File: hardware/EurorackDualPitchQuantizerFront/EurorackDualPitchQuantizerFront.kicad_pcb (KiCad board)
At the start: 2 copper layers, 48 x 110 mm, 67 parts, among them J1 Conn_01x12_Male, J10 Conn_01x04_Male, J11 AudioJack2, J12 AudioJack2, J13 Conn_01x02_Male, J2 Conn_01x01_Male, J3 Conn_01x02_Male, J4 Conn_01x02_Male, J5 AudioJack2, J6 AudioJack2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

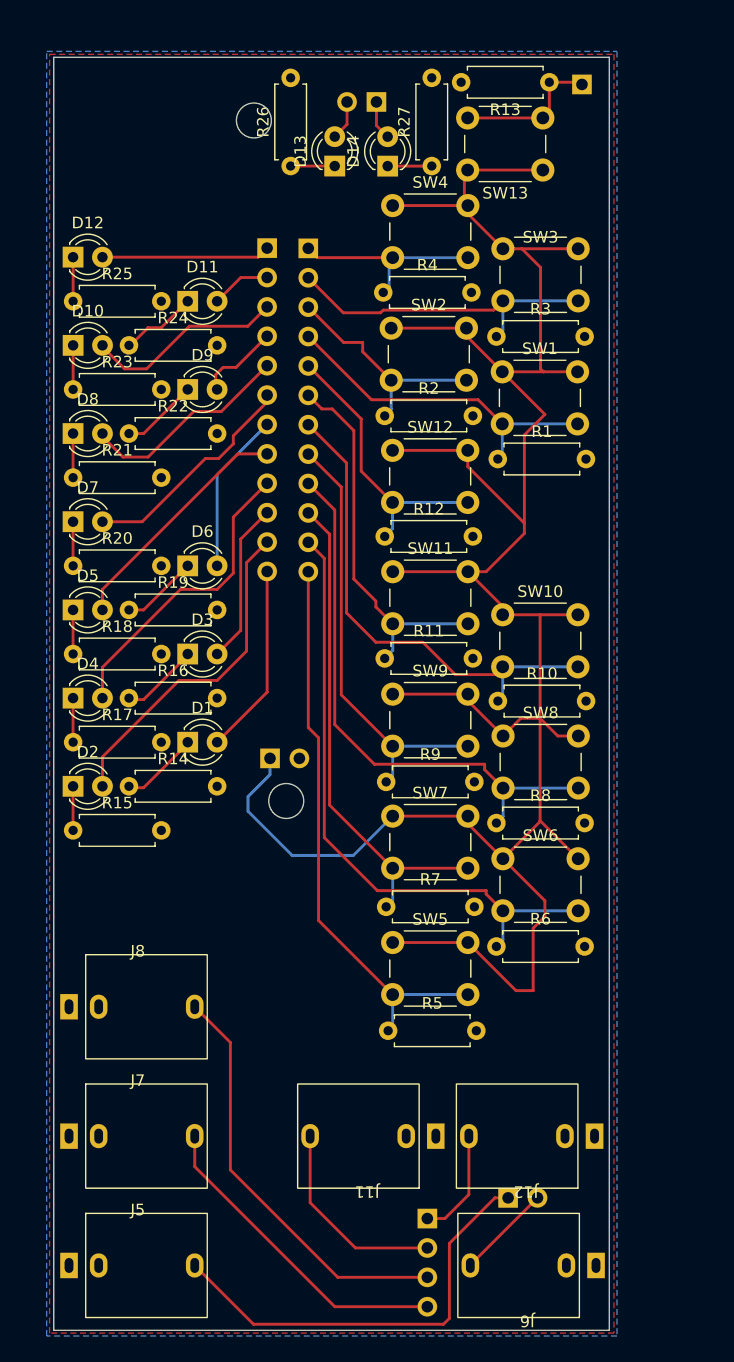
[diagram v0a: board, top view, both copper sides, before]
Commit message: made another version that is not viable since it is too tall
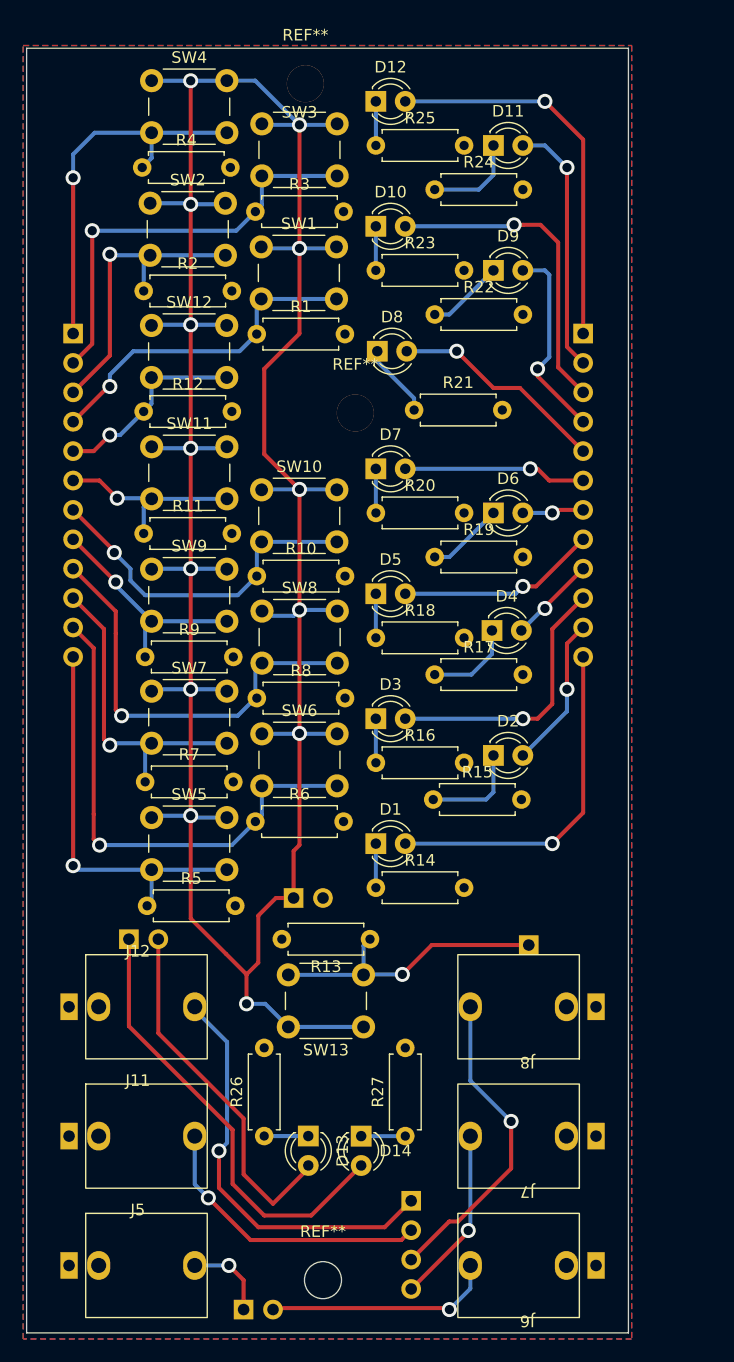
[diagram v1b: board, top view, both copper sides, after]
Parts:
- added REF**: MountingHole_3.2mm_M3, MountingHole:MountingHole_3.2mm_M3, F.Cu at (38.6, 123.4)
- added REF**: MountingHole_3.2mm_M3, MountingHole:MountingHole_3.2mm_M3, F.Cu at (37.1, 20.1)
- added REF**: MountingHole_3.2mm_M3, MountingHole:MountingHole_3.2mm_M3, F.Cu at (41.4, 48.5)
- J11, J12, J5, J6, J7, J8: value AudioJack2 -> AudioJack2_SwitchT
- moved D13 83.8 mm to (37.3, 111.0), turned to -90 degrees
- moved D14 83.8 mm to (41.9, 111.0), turned to -90 degrees
- moved R26 83.8 mm to (33.5, 111.0)
- moved R27 83.8 mm to (45.7, 111.0)
- moved R13 75.6 mm to (42.7, 94.0)
- moved SW13 75.6 mm to (42.1, 101.6)
- moved J13 75.4 mm to (21.8, 94.0), turned to -90 degrees
- moved J2 74.5 mm to (56.4, 94.5)
- moved D4 36.7 mm to (53.2, 67.3)
- moved D2 36.4 mm to (53.3, 78.1)
- moved J12 35.3 mm to (22.6, 99.8), turned to 0 degrees
- moved J7 33.7 mm to (56.3, 111.0), turned to 180 degrees
- moved J8 33.7 mm to (56.3, 99.8), turned to 180 degrees
- moved R17 31.8 mm to (48.3, 71.1)
- moved R15 31.2 mm to (48.1, 81.9)
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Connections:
- J11 pad S: Net-(J10-Pad2) -> GND
- J11 pad T: GND -> Net-(J10-Pad2)
- J12 pad S: Net-(J10-Pad1) -> GND
- J12 pad T: GND -> Net-(J10-Pad1)
- J5 pad S: Net-(J4-Pad1) -> GND
- J5 pad T: GND -> Net-(J4-Pad1)
- J6 pad S: Net-(J4-Pad2) -> GND
- J6 pad T: GND -> Net-(J4-Pad2)
- J7 pad S: Net-(J10-Pad4) -> GND
- J7 pad T: GND -> Net-(J10-Pad4)
- J8 pad S: Net-(J10-Pad3) -> GND
- J8 pad T: GND -> Net-(J10-Pad3)
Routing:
- net +5V: track 218.2 -> 258.5 mm, vias 0 -> 13
- net Net-(D14-Pad2): track 3.40 -> 38.9 mm
- net Net-(J4-Pad1): track 37.5 -> 7.29 mm, vias 0 -> 1
- net Net-(D13-Pad2): track 3.44 -> 31.5 mm
- net Net-(J10-Pad1): track 9.88 -> 36.1 mm, vias 0 -> 1
- net Net-(D12-Pad2): track 14.3 -> 33.5 mm, vias 0 -> 1
- net Net-(D4-Pad2): track 26.3 -> 7.63 mm, vias 0 -> 1
- net Net-(J1-Pad8): track 38.1 -> 19.7 mm, vias 0 -> 1
- net Net-(D11-Pad2): track 5.17 -> 22.1 mm, vias 0 -> 1
- net Net-(J1-Pad10): track 43.8 -> 27.8 mm, vias 0 -> 1
- net Net-(J1-Pad1): track 17.0 -> 32.9 mm, vias 0 -> 1
- net Net-(J1-Pad6): track 33.1 -> 17.2 mm, vias 0 -> 1
- net Net-(D2-Pad2): track 28.9 -> 13.2 mm, vias 0 -> 1
- net Net-(J1-Pad12): track 49.3 -> 34.7 mm, vias 0 -> 1
- net Net-(D1-Pad2): track 16.5 -> 29.9 mm, vias 0 -> 1
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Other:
- board size 48 x 110 mm -> 52 x 111 mm

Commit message: Got Rev 1.2 complete. It should be manufacturable and fit into eurorack standards.
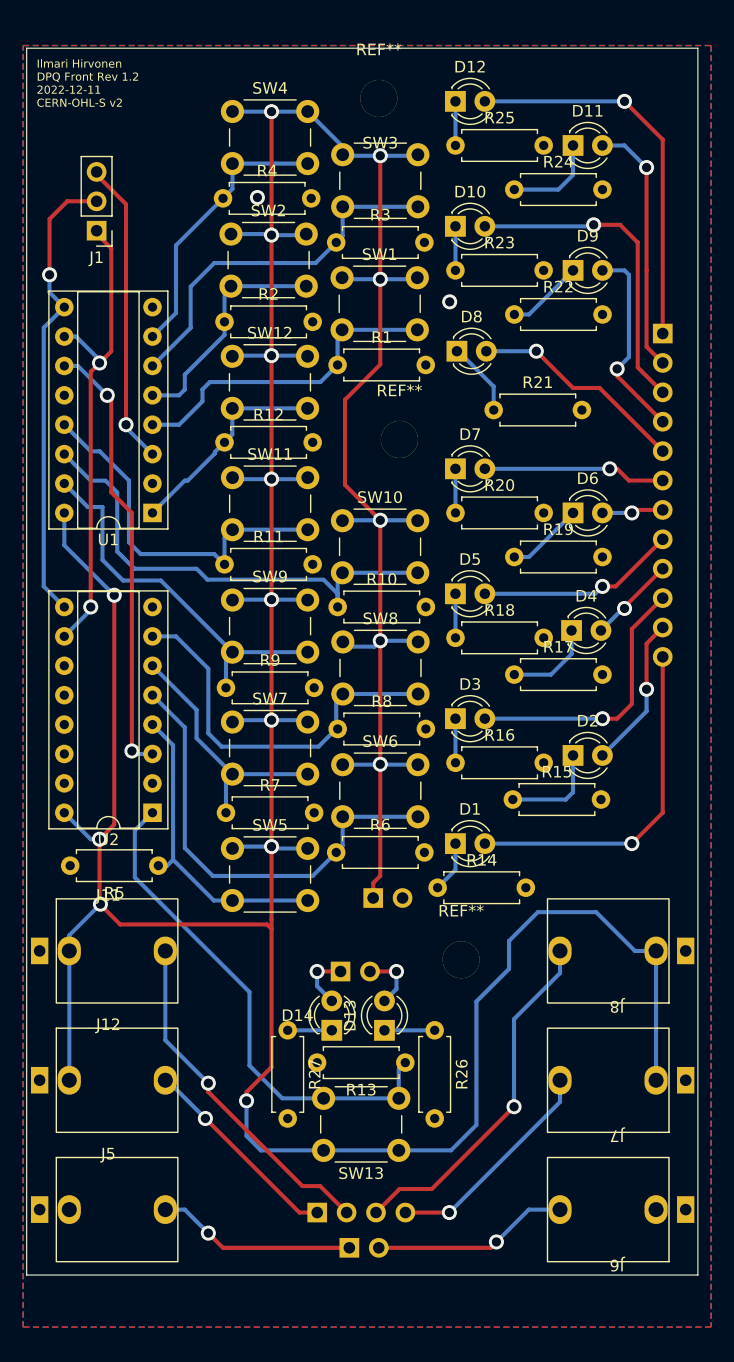
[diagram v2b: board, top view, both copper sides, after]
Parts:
- removed J2: Conn_01x01_Male, Connector_PinHeader_2.54mm:PinHeader_1x01_P2.54mm_Vertical
- removed the REF** at (38.6, 123.4)
- removed the REF** at (37.1, 20.1)
- removed the REF** at (41.4, 48.5)
- added REF**: MountingHole_3.2mm_M3, MountingHole:MountingHole_3.2mm_M3, F.Cu at (43.4, 21.3)
- added REF**: MountingHole_3.2mm_M3, MountingHole:MountingHole_3.2mm_M3, F.Cu at (50.5, 95.8)
- added REF**: MountingHole_3.2mm_M3, MountingHole:MountingHole_3.2mm_M3, F.Cu at (45.2, 50.8)
- added U1: 4021, Package_DIP:DIP-16_W7.62mm_Socket, F.Cu at (23.9, 57.1)
- added U2: 4021, Package_DIP:DIP-16_W7.62mm_Socket, F.Cu at (23.9, 83.1)
- J1: value Conn_01x12_Male -> Conn_01x03_Female; footprint Connector_PinHeader_2.54mm:PinHeader_1x12_P2.54mm_Vertical -> Connector_PinHeader_2.54mm:PinHeader_1x03_P2.54mm_Vertical; moved to F.Cu
- moved J13 18.5 mm to (40.1, 96.8)
- moved R26 17.3 mm to (48.3, 101.9), turned to -90 degrees
- moved J11 16.2 mm to (20.1, 95.0)
- moved R27 13.7 mm to (35.6, 101.9), turned to -90 degrees
- moved D13 11.3 mm to (43.9, 101.9), turned to 90 degrees
- moved SW13 11.1 mm to (45.2, 112.2)
- moved R13 11.1 mm to (45.7, 104.6)
- moved J4 10.6 mm to (40.9, 120.7)
- moved D14 9.49 mm to (39.4, 101.9), turned to 90 degrees
- moved J6 9.13 mm to (64.0, 117.3)
- moved J7 9.13 mm to (64.0, 106.2)
- moved J8 9.13 mm to (64.0, 95.0)
- moved J1 9.11 mm to (19.1, 32.8)
- moved J10 8.18 mm to (38.1, 117.6), turned to -90 degrees
- moved R4 7.48 mm to (30.0, 30.0)
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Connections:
- J11 pad TN: GND -> +5V
- J12 pad TN: GND -> +5V
- J7 pad TN: GND -> +5V
- J8 pad TN: GND -> +5V
- R1 pad 1: Net-(J1-Pad4) -> /B4
- R10 pad 1: Net-(J1-Pad7) -> /B6
- R11 pad 1: Net-(J1-Pad6) -> /B5
- R12 pad 1: Net-(J1-Pad5) -> /B8
- R2 pad 1: Net-(J1-Pad3) -> /B3
- R3 pad 1: Net-(J1-Pad2) -> /B2
- R4 pad 1: Net-(J1-Pad1) -> /B1
- R5 pad 1: Net-(J1-Pad12) -> /B12
- R6 pad 1: Net-(J1-Pad11) -> /B11
- R7 pad 1: Net-(J1-Pad10) -> /B10
- R8 pad 1: Net-(J1-Pad9) -> /B9
- R9 pad 1: Net-(J1-Pad8) -> /B7
- SW1 pad 2: Net-(J1-Pad4) -> /B4
- SW10 pad 2: Net-(J1-Pad7) -> /B6
- SW11 pad 2: Net-(J1-Pad6) -> /B5
- SW12 pad 2: Net-(J1-Pad5) -> /B8
- SW2 pad 2: Net-(J1-Pad3) -> /B3
- SW3 pad 2: Net-(J1-Pad2) -> /B2
- SW4 pad 2: Net-(J1-Pad1) -> /B1
- SW5 pad 2: Net-(J1-Pad12) -> /B12
- SW6 pad 2: Net-(J1-Pad11) -> /B11
- SW7 pad 2: Net-(J1-Pad10) -> /B10
- SW8 pad 2: Net-(J1-Pad9) -> /B9
- SW9 pad 2: Net-(J1-Pad8) -> /B7
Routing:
- net +5V: track 258.5 -> 377.8 mm, vias 13 -> 16
- net Net-(J1-Pad11): track 43.9 -> 0.00 mm, vias 1 -> 0
- net /B6: track 0.00 -> 42.4 mm
- net /B11: track 0.00 -> 39.1 mm
- net Net-(U1-Pad11): track 0.00 -> 38.3 mm, vias 0 -> 2
- net Net-(J1-Pad9): track 36.4 -> 0.00 mm, vias 1 -> 0
- net Net-(J1-Pad12): track 34.7 -> 0.00 mm, vias 1 -> 0
- net Net-(D14-Pad2): track 38.9 -> 5.09 mm, vias 0 -> 1
- net /B9: track 0.00 -> 33.5 mm
- net /B7: track 0.00 -> 33.1 mm
- net /B2: track 0.00 -> 32.2 mm
- net /B5: track 0.00 -> 31.8 mm
- net Net-(J1-Pad7): track 29.9 -> 0.00 mm, vias 1 -> 0
- net Net-(J1-Pad4): track 29.3 -> 0.00 mm, vias 1 -> 0
- net /B4: track 0.00 -> 28.4 mm
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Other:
- board size 52 x 111 mm -> 58 x 106 mm
- board text added: "Ilmari Hirvonen DPQ Front Rev 1.2 2022-12-11 CERN-OHL-S v2"
